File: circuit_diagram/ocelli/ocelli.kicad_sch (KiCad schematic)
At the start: 114 parts, among them J1 Conn_01x06, J2 Conn_01x06, J3 Conn_01x06, J4 Conn_01x06, J5 Conn_01x08, J6 Conn_01x02, J7 Conn_01x02, Q1 BSS138, Q10 BSS138, Q2 ST-1KL3A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

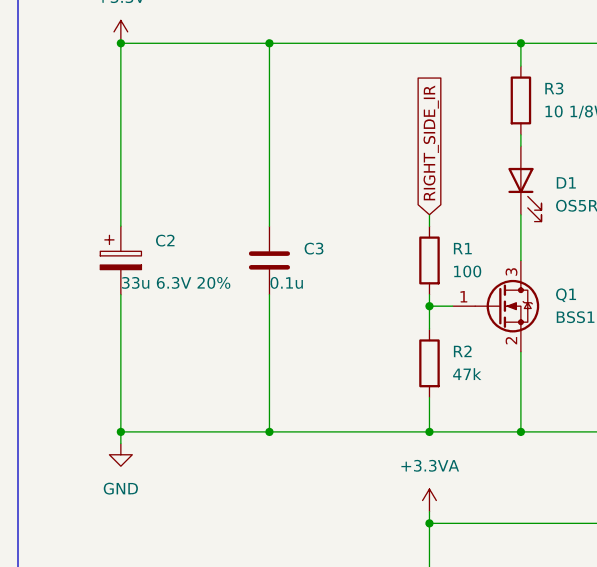
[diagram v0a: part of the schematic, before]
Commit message: 使用するコンデンサを変更
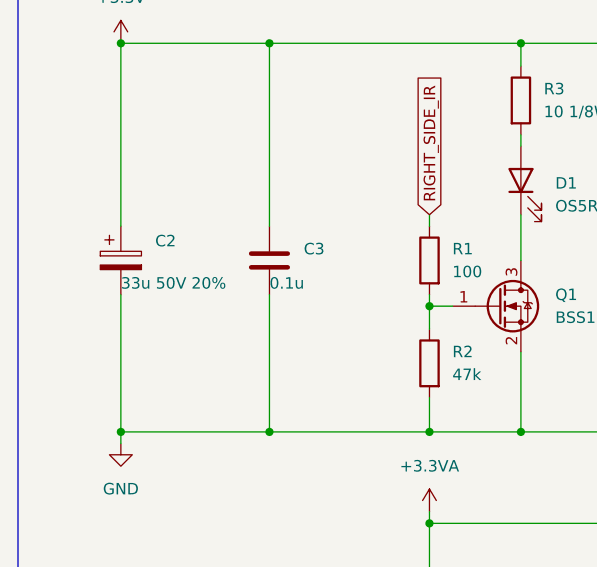
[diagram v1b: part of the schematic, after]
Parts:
- C2: value 33u 6.3V 20% -> 33u 50V 20%; url https://www.digikey.jp/ja/products/detail/murata-electronic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 -> https://akizukidenshi.com/catalog/g/gP-16749/
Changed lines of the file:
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@@
       (effects (font (size 1.27 1.27)) (justify left))
     )
-    (property "Value" "33u 6.3V 20%" (id 1) (at 24.13 96.52 0)
+    (property "Value" "33u 50V 20%" (id 1) (at 24.13 96.52 0)
       (effects (font (size 1.27 1.27)) (justify left))
     )
@@
       (effects (font (size 1.27 1.27)) hide)
     )
-    (property "url" "https://www.digikey.jp/ja/products/detail/murata-electronics/GRT32DR60J336ME01K/13904806" (id 4) (at 24.13 93.98 0)
+    (property "url" "https://akizukidenshi.com/catalog/g/gP-16749/" (id 4) (at 24.13 93.98 0)
       (effects (font (size 1.27 1.27)) hide)
     )
@@
     )
     (path "/6ec1fbce-5ed9-49a9-b67b-d64bef25ff62"
-      (reference "C2") (unit 1) (value "33u 6.3V 20%") (footprint "")
+      (reference "C2") (unit 1) (value "33u 50V 20%") (footprint "")
     )
     (path "/230be6a4-af26-49e4-a244-e2dbf0a97ea4"

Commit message: フットプリント割当完了
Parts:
- BT1: footprint (none) -> ocelli_lib:pad_01x02
- C2: footprint (none) -> Capacitor_SMD:CP_Elec_6.3x7.7
- D1, D2, D3, D5: footprint (none) -> LED_THT:LED_D5.0mm_Horizontal_O1.27mm_Z3.0mm; url (none) -> https://akizukidenshi.com/catalog/g/gI-04768/
- D4, D6, D7: value LED -> OSBL1608C1A; url (none) -> https://akizukidenshi.com/catalog/g/gI-03982/
- D8, D9: value LED -> OSYL1608C1A; url (none) -> https://akizukidenshi.com/catalog/g/gI-03984/
- FB1: footprint (none) -> Inductor_SMD:L_0603_1608Metric_Pad1.05x0.95mm_HandSolder; url (none) -> https://www.digikey.jp/ja/products/detail/bourns-inc/MZ1608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
- J1, J2, J3, J4: footprint (none) -> ocelli_lib:encoder_board_pad; url (none) -> none
- J5: footprint (none) -> Connector_PinSocket_1.27mm:PinSocket_1x08_P1.27mm_Vertical
- J6, J7: footprint (none) -> ocelli_lib:pad_01x02; url (none) -> none
- LS1: footprint (none) -> Buzzer_Beeper:Buzzer_Murata_PKMCS0909E; url (none) -> https://akizukidenshi.com/catalog/g/gP-14238/
- Q1, Q10, Q5, Q7, Q9: footprint (none) -> Package_TO_SOT_SMD:SOT-23; url (none) -> https://akizukidenshi.com/catalog/g/gI-04232/
- Q2, Q4, Q6, Q8: footprint (none) -> LED_THT:LED_D5.0mm_Horizontal_O3.81mm_Z9.0mm; url (none) -> https://www.rt-shop.jp/index.php?main_page=product_info&pro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
- Q3: footprint (none) -> Package_TO_SOT_SMD:TO-252-2; url (none) -> https://akizukidenshi.com/catalog/g/gI-13964/
- RV1: footprint (none) -> ocelli_lib:ST4ETB103
- SW1: footprint (none) -> ocelli_lib:SSSS213202; url (none) -> https://akizukidenshi.com/catalog/g/gP-05043/
- SW2, SW3, SW4: value TS-06104 -> TVAF06-A020B-R; footprint (none) -> ocelli_lib:TVAF06-A020B-R; symbol Switch:SW_MEC_5E -> Switch:SW_MEC_5G; url (none) -> https://akizukidenshi.com/catalog/g/gP-14888/
- SW5, SW6: value SW_Push -> TVAF06-A020B-R; footprint (none) -> ocelli_lib:TVAF06-A020B-R; url (none) -> https://akizukidenshi.com/catalog/g/gP-14888/
- U1: footprint (none) -> Package_TO_SOT_SMD:TO-252-2; url (none) -> https://akizukidenshi.com/catalog/g/gI-11299/
- U2, U3: url (none) -> https://www.mouser.jp/ProductDetail/ams/AS5055A-BQFT?qs=Ifo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
- U4: footprint (none) -> Package_DFN_QFN:HVQFN-24-1EP_4x4mm_P0.5mm_EP2.1x2.1mm; url (none) -> https://www.mouser.jp/ProductDetail/TDK-InvenSense/ICM-2064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
- U5: url (none) -> https://akizukidenshi.com/catalog/g/gI-13219/
- U6: footprint (none) -> ocelli_lib:DRV8835; url (none) -> https://akizukidenshi.com/catalog/g/gK-09848/
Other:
- moved on the sheet: C18, J5, R24, R31, R32, R33, SW5, SW6

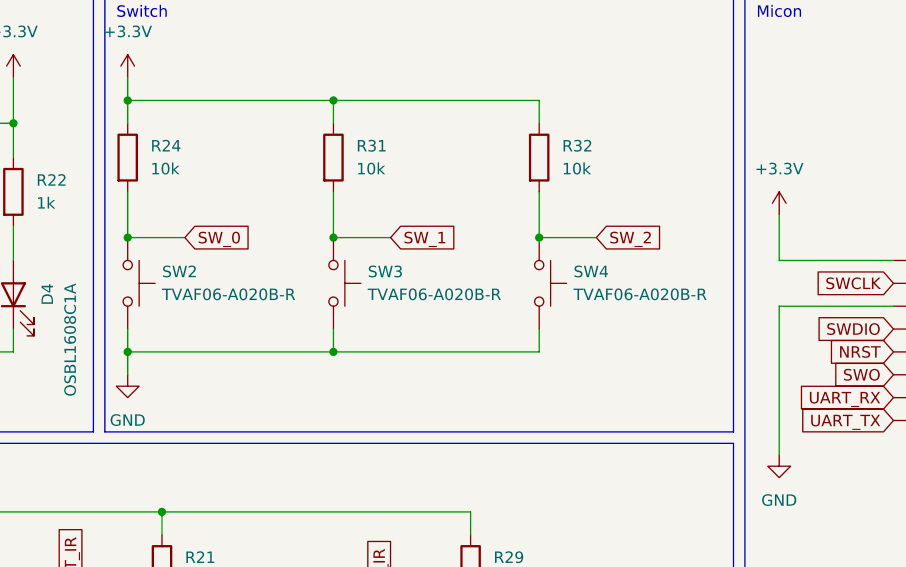
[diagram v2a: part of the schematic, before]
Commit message: モータマウント等のスケッチ追加
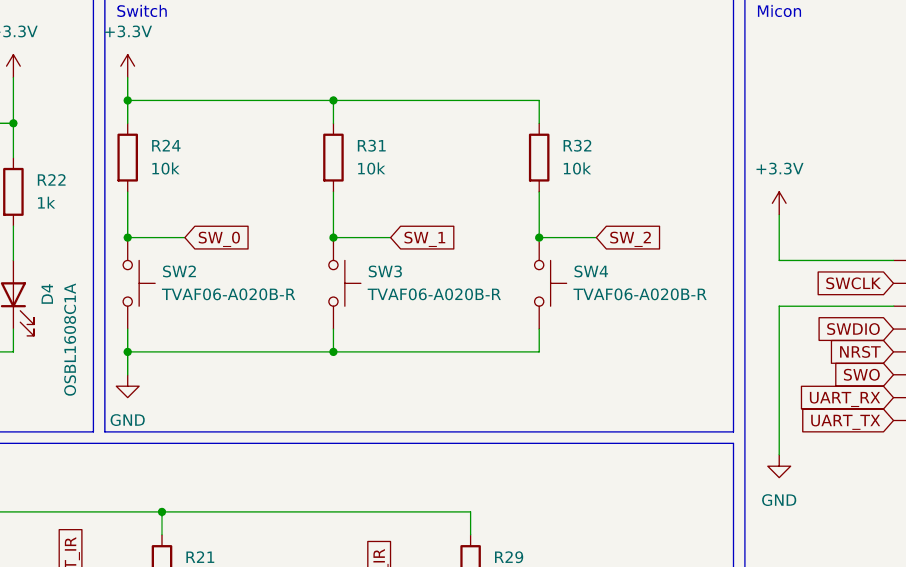
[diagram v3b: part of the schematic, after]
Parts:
- removed SW2, SW3, SW4: TVAF06-A020B-R, ocelli_lib:TVAF06-A020B-R, symbol Switch:SW_MEC_5G
- added SW2, SW3, SW4: TVAF06-A020B-R, ocelli_lib:TVAF06-A020B-R, symbol Switch:SW_Push
- Q2, Q4, Q6, Q8: footprint LED_THT:LED_D5.0mm_Horizontal_O3.81mm_Z9.0mm -> ocelli_lib:ST-1KL3A
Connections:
- net GND: now also SW2.2, SW3.2, SW4.2
- net SW_0: now also SW2.1
- net SW_1: now also SW3.1
- net SW_2: now also SW4.1
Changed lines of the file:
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@@
   (junction (at 106.68 161.29) (diameter 0) (color 0 0 0 0)
   )
-  (junction (at 133.35 39.37) (diameter 0) (color 0 0 0 0)
-  )
   (junction (at 256.54 127) (diameter 0) (color 0 0 0 0)
   )
@@
   (junction (at 140.97 161.29) (diameter 0) (color 0 0 0 0)
   )
+  (junction (at 133.35 39.37) (diameter 0) (color 0 0 0 0)
+  )
   (junction (at 85.09 26.67) (diameter 0) (color 0 0 0 0)
   )
@@
   (junction (at 367.03 132.08) (diameter 0) (color 0 0 0 0)
   )
-  (junction (at 156.21 39.37) (diameter 0) (color 0 0 0 0)
-  )
   (junction (at 241.3 88.9) (diameter 0) (color 0 0 0 0)
   )
@@
   (junction (at 364.49 165.1) (diameter 0) (color 0 0 0 0)
   )
+  (junction (at 156.21 39.37) (diameter 0) (color 0 0 0 0)
+  )
   (junction (at 345.44 171.45) (diameter 0) (color 0 0 0 0)
   )
@@
     (pin "1")
   )
+  (symbol (lib_id "Switch:SW_Push") (at 156.21 44.45 270) (unit 1)
+    (in_bom yes) (on_board yes) (fields_autoplaced)
+    (property "Reference" "SW3" (id 0) (at 160.02 43.1799 90)
+      (effects (font (size 1.27 1.27)) (justify left))
+    )
+    (property "Value" "TVAF06-A020B-R" (id 1) (at 160.02 45.7199 90)
+      (effects (font (size 1.27 1.27)) (justify left))
+    )
+    (property "Footprint" "ocelli_lib:TVAF06-A020B-R" (id 2) (at 161.29 44.45 0)
+      (effects (font (size 1.27 1.27)) hide)
+    )
+    (property "Datasheet" "~" (id 3) (at 161.29 44.45 0)
+      (effects (font (size 1.27 1.27)) hide)
+    )
+    (property "url" "https://akizukidenshi.com/catalog/g/gP-14888/" (id 4) (at 156.21 44.45 0)
+      (effects (font (size 1.27 1.27)) hide)
+    )
+    (pin "1")
+    (pin "2")
+  )
   (symbol (lib_id "Device:C") (at 107.95 39.37 0) (unit 1)
     (in_bom yes) (on_board yes)
@@
       (effects (font (size 1.27 1.27)) (justify left))
     )
-    (property "Footprint" "LED_THT:LED_D5.0mm_Horizontal_O3.81mm_Z9.0mm" (id 2) (at 163.83 134.62 0)
+    (property "Footprint" "ocelli_lib:ST-1KL3A" (id 2) (at 163.83 134.62 0)
       (effects (font (size 1.27 1.27)) hide)
     )
@@
     (pin "2")
   )
-  (symbol (lib_id "Switch:SW_MEC_5G") (at 179.07 44.45 270) (unit 1)
-    (in_bom yes) (on_board yes)
-    (property "Reference" "SW4" (id 0) (at 182.88 43.18 90)
-      (effects (font (size 1.27 1.27)) (justify left))
-    )
-    (property "Value" "TVAF06-A020B-R" (id 1) (at 182.88 45.72 90)
-      (effects (font (size 1.27 1.27)) (justify left))
-    )
-    (property "Footprint" "ocelli_lib:TVAF06-A020B-R" (id 2) (at 184.15 44.45 0)
-      (effects (font (size 1.27 1.27)) hide)
-    )
-    (property "Datasheet" "http://www.apem.com/int/index.php?controller=attachment&id_attachment=488" (id 3) (at 184.15 44.45 0)
-      (effects (font (size 1.27 1.27)) hide)
-    )
-    (property "url" "https://akizukidenshi.com/catalog/g/gP-14888/" (id 4) (at 179.07 44.45 0)
-      (effects (font (size 1.27 1.27)) hide)
-    )
-    (pin "1")
-    (pin "3")
-    (pin "2")
-    (pin "4")
-  )
   (symbol (lib_id "Device:R") (at 68.58 76.2 0) (unit 1)
     (in_bom yes) (on_board yes) (fields_autoplaced)
@@
     (pin "3")
   )
-  (symbol (lib_id "Switch:SW_MEC_5G") (at 133.35 44.45 270) (unit 1)
-    (in_bom yes) (on_board yes)
-    (property "Reference" "SW2" (id 0) (at 137.16 43.18 90)
-      (effects (font (size 1.27 1.27)) (justify left))
-    )
-    (property "Value" "TVAF06-A020B-R" (id 1) (at 137.16 45.72 90)
-      (effects (font (size 1.27 1.27)) (justify left))
-    )
-    (property "Footprint" "ocelli_lib:TVAF06-A020B-R" (id 2) (at 138.43 44.45 0)
-      (effects (font (size 1.27 1.27)) hide)
-    )
-    (property "Datasheet" "http://www.apem.com/int/index.php?controller=attachment&id_attachment=488" (id 3) (at 138.43 44.45 0)
-      (effects (font (size 1.27 1.27)) hide)
-    )
-    (property "url" "https://akizukidenshi.com/catalog/g/gP-14888/" (id 4) (at 133.35 44.45 0)
-      (effects (font (size 1.27 1.27)) hide)
-    )
-    (pin "1")
-    (pin "3")
-    (pin "2")
-    (pin "4")
-  )
   (symbol (lib_id "power:GND") (at 180.34 248.92 0) (unit 1)
     (in_bom yes) (on_board yes) (fields_autoplaced)
@@
     (pin "2")
   )
+  (symbol (lib_id "Switch:SW_Push") (at 179.07 44.45 270) (unit 1)
+    (in_bom yes) (on_board yes) (fields_autoplaced)
+    (property "Reference" "SW4" (id 0) (at 182.88 43.1799 90)
+      (effects (font (size 1.27 1.27)) (justify left))
+    )
+    (property "Value" "TVAF06-A020B-R" (id 1) (at 182.88 45.7199 90)
+      (effects (font (size 1.27 1.27)) (justify left))
+    )
+    (property "Footprint" "ocelli_lib:TVAF06-A020B-R" (id 2) (at 184.15 44.45 0)
+      (effects (font (size 1.27 1.27)) hide)
+    )
+    (property "Datasheet" "~" (id 3) (at 184.15 44.45 0)
+      (effects (font (size 1.27 1.27)) hide)
+    )
+    (property "url" "https://akizukidenshi.com/catalog/g/gP-14888/" (id 4) (at 179.07 44.45 0)
+      (effects (font (size 1.27 1.27)) hide)
+    )
+    (pin "1")
+    (pin "2")
+  )
   (symbol (lib_id "Device:Q_Photo_NPN") (at 55.88 137.16 0) (unit 1)
     (in_bom yes) (on_board yes) (fields_autoplaced)
@@
       (effects (font (size 1.27 1.27)) (justify left))
     )
-    (property "Footprint" "LED_THT:LED_D5.0mm_Horizontal_O3.81mm_Z9.0mm" (id 2) (at 60.96 134.62 0)
+    (property "Footprint" "ocelli_lib:ST-1KL3A" (id 2) (at 60.96 134.62 0)
       (effects (font (size 1.27 1.27)) hide)
     )
@@
     (pin "6")
   )
+  (symbol (lib_id "Switch:SW_Push") (at 133.35 44.45 270) (unit 1)
+    (in_bom yes) (on_board yes) (fields_autoplaced)
+    (property "Reference" "SW2" (id 0) (at 137.16 43.1799 90)
+      (effects (font (size 1.27 1.27)) (justify left))
+    )
+    (property "Value" "TVAF06-A020B-R" (id 1) (at 137.16 45.7199 90)
+      (effects (font (size 1.27 1.27)) (justify left))
+    )
+    (property "Footprint" "ocelli_lib:TVAF06-A020B-R" (id 2) (at 138.43 44.45 0)
+      (effects (font (size 1.27 1.27)) hide)
+    )
+    (property "Datasheet" "~" (id 3) (at 138.43 44.45 0)
+      (effects (font (size 1.27 1.27)) hide)
+    )
+    (property "url" "https://akizukidenshi.com/catalog/g/gP-14888/" (id 4) (at 133.35 44.45 0)
+      (effects (font (size 1.27 1.27)) hide)
+    )
+    (pin "1")
+    (pin "2")
+  )
   (symbol (lib_id "Device:C") (at 226.06 105.41 0) (unit 1)
     (in_bom yes) (on_board yes)
@@
       (effects (font (size 1.27 1.27)) (justify left))
     )
-    (property "Footprint" "LED_THT:LED_D5.0mm_Horizontal_O3.81mm_Z9.0mm" (id 2) (at 95.25 134.62 0)
+    (property "Footprint" "ocelli_lib:ST-1KL3A" (id 2) (at 95.25 134.62 0)
       (effects (font (size 1.27 1.27)) hide)
     )
@@
       (effects (font (size 1.27 1.27)) (justify left))
     )
-    (property "Footprint" "LED_THT:LED_D5.0mm_Horizontal_O3.81mm_Z9.0mm" (id 2) (at 129.54 134.62 0)
+    (property "Footprint" "ocelli_lib:ST-1KL3A" (id 2) (at 129.54 134.62 0)
       (effects (font (size 1.27 1.27)) hide)
     )
@@
     (pin "1")
   )
-  (symbol (lib_id "Switch:SW_MEC_5G") (at 156.21 44.45 270) (unit 1)
-    (in_bom yes) (on_board yes)
-    (property "Reference" "SW3" (id 0) (at 160.02 43.18 90)
-      (effects (font (size 1.27 1.27)) (justify left))
-    )
-    (property "Value" "TVAF06-A020B-R" (id 1) (at 160.02 45.72 90)
-      (effects (font (size 1.27 1.27)) (justify left))
-    )
-    (property "Footprint" "ocelli_lib:TVAF06-A020B-R" (id 2) (at 161.29 44.45 0)
-      (effects (font (size 1.27 1.27)) hide)
-    )
-    (property "Datasheet" "http://www.apem.com/int/index.php?controller=attachment&id_attachment=488" (id 3) (at 161.29 44.45 0)
-      (effects (font (size 1.27 1.27)) hide)
-    )
-    (property "url" "https://akizukidenshi.com/catalog/g/gP-14888/" (id 4) (at 156.21 44.45 0)
-      (effects (font (size 1.27 1.27)) hide)
-    )
-    (pin "1")
-    (pin "3")
-    (pin "2")
-    (pin "4")
-  )
   (symbol (lib_id "power:GND") (at 251.46 67.31 0) (unit 1)
     (in_bom yes) (on_board yes) (fields_autoplaced)
@@
     )
     (path "/4c45e7b5-910f-4a6e-9672-ff25f0fd35cc"
-      (reference "Q2") (unit 1) (value "ST-1KL3A") (footprint "LED_THT:LED_D5.0mm_Horizontal_O3.81mm_Z9.0mm")
+      (reference "Q2") (unit 1) (value "ST-1KL3A") (footprint "ocelli_lib:ST-1KL3A")
     )
     (path "/435dadaa-c7e3-4c4f-bc2c-12a7e04a6abf"
@@
     )
     (path "/78380d7a-7050-4fa4-83b0-a213bce03f9b"
-      (reference "Q4") (unit 1) (value "ST-1KL3A") (footprint "LED_THT:LED_D5.0mm_Horizontal_O3.81mm_Z9.0mm")
+      (reference "Q4") (unit 1) (value "ST-1KL3A") (footprint "ocelli_lib:ST-1KL3A")
     )
     (path "/94ce2d53-3690-4996-b763-8e3b6108af0e"
@@
     )
     (path "/9f5b177c-9103-4a89-b330-896e69e5904b"
-      (reference "Q6") (unit 1) (value "ST-1KL3A") (footprint "LED_THT:LED_D5.0mm_Horizontal_O3.81mm_Z9.0mm")
+      (reference "Q6") (unit 1) (value "ST-1KL3A") (footprint "ocelli_lib:ST-1KL3A")
     )
     (path "/75084031-bbcc-406c-9e18-9391703c81e5"
@@
     )
     (path "/32aec8ec-50f2-4728-8cae-a80e6b28ac7b"
-      (reference "Q8") (unit 1) (value "ST-1KL3A") (footprint "LED_THT:LED_D5.0mm_Horizontal_O3.81mm_Z9.0mm")
+      (reference "Q8") (unit 1) (value "ST-1KL3A") (footprint "ocelli_lib:ST-1KL3A")
     )
     (path "/1e2c13ea-b331-4134-badd-72868480756e"
@@
       (reference "SW1") (unit 1) (value "SW_SPDT") (footprint "ocelli_lib:SSSS213202")
     )
-    (path "/43862056-8f38-4e81-aa22-d1ec7c5a2da3"
+    (path "/58cb58b3-37ed-4568-8a79-346a92967709"
       (reference "SW2") (unit 1) (value "TVAF06-A020B-R") (footprint "ocelli_lib:TVAF06-A020B-R")
     )
-    (path "/f6fb72fb-63c0-4b68-b993-96a8461decb2"
+    (path "/0a2cfeda-4aaf-49a5-8ecc-a99df2e06d58"
       (reference "SW3") (unit 1) (value "TVAF06-A020B-R") (footprint "ocelli_lib:TVAF06-A020B-R")
     )
-    (path "/3efb25df-c3a7-4246-af1c-174de46e1c02"
+    (path "/4b3350b0-8afe-4e06-a639-1386f446f29e"
       (reference "SW4") (unit 1) (value "TVAF06-A020B-R") (footprint "ocelli_lib:TVAF06-A020B-R")
     )

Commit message: 一通りパターンを繋いだ
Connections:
- net DIR_L: now also U5.41 (PA8); no longer U5.43 (PA10)
- net DIR_R: now also U5.43 (PA10); no longer U5.44 (PA11)
- net LEFT_FRONT_AD: now also U5.27 (PB1); no longer U5.26 (PB0)
- net LEFT_SIDE_AD: now also U5.26 (PB0); no longer U5.27 (PB1)
- net PWM_L: now also U5.42 (PA9); no longer U5.41 (PA8)
- net PWM_R: now also U5.44 (PA11); no longer U5.42 (PA9)
- net RIGHT_FRONT_AD: now also U5.24 (PC4); no longer U5.25 (PC5)
- net RIGHT_SIDE_AD: now also U5.25 (PC5); no longer U5.24 (PC4)
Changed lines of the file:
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@@
     )
   )
-  (global_label "RIGHT_SIDE_AD" (shape input) (at 233.68 185.42 180) (fields_autoplaced)
-    (effects (font (size 1.27 1.27)) (justify right))
-    (property "Intersheet References" "${INTERSHEET_REFS}" (id 0) (at 217.2969 185.4994 0)
+  (global_label "RIGHT_SIDE_AD" (shape input) (at 233.68 187.96 180) (fields_autoplaced)
+    (effects (font (size 1.27 1.27)) (justify right))
+    (property "Intersheet References" "${INTERSHEET_REFS}" (id 0) (at 217.2969 188.0394 0)
       (effects (font (size 1.27 1.27)) (justify right) hide)
     )
@@
     )
   )
-  (global_label "LEFT_FRONT_AD" (shape input) (at 269.24 175.26 0) (fields_autoplaced)
-    (effects (font (size 1.27 1.27)) (justify left))
-    (property "Intersheet References" "${INTERSHEET_REFS}" (id 0) (at 286.1674 175.1806 0)
-      (effects (font (size 1.27 1.27)) (justify left) hide)
-    )
-  )
-  (global_label "RIGHT_FRONT_AD" (shape input) (at 233.68 187.96 180) (fields_autoplaced)
-    (effects (font (size 1.27 1.27)) (justify right))
-    (property "Intersheet References" "${INTERSHEET_REFS}" (id 0) (at 215.5431 188.0394 0)
+  (global_label "LEFT_FRONT_AD" (shape input) (at 269.24 177.8 0) (fields_autoplaced)
+    (effects (font (size 1.27 1.27)) (justify left))
+    (property "Intersheet References" "${INTERSHEET_REFS}" (id 0) (at 286.1674 177.7206 0)
+      (effects (font (size 1.27 1.27)) (justify left) hide)
+    )
+  )
+  (global_label "RIGHT_FRONT_AD" (shape input) (at 233.68 185.42 180) (fields_autoplaced)
+    (effects (font (size 1.27 1.27)) (justify right))
+    (property "Intersheet References" "${INTERSHEET_REFS}" (id 0) (at 215.5431 185.4994 0)
       (effects (font (size 1.27 1.27)) (justify right) hide)
     )
@@
     )
   )
-  (global_label "DIR_L" (shape input) (at 269.24 157.48 0) (fields_autoplaced)
-    (effects (font (size 1.27 1.27)) (justify left))
-    (property "Intersheet References" "${INTERSHEET_REFS}" (id 0) (at 276.7936 157.4006 0)
+  (global_label "DIR_L" (shape input) (at 269.24 152.4 0) (fields_autoplaced)
+    (effects (font (size 1.27 1.27)) (justify left))
+    (property "Intersheet References" "${INTERSHEET_REFS}" (id 0) (at 276.7936 152.3206 0)
       (effects (font (size 1.27 1.27)) (justify left) hide)
     )
@@
     )
   )
-  (global_label "LEFT_SIDE_AD" (shape input) (at 269.24 177.8 0) (fields_autoplaced)
-    (effects (font (size 1.27 1.27)) (justify left))
-    (property "Intersheet References" "${INTERSHEET_REFS}" (id 0) (at 284.4136 177.7206 0)
+  (global_label "LEFT_SIDE_AD" (shape input) (at 269.24 175.26 0) (fields_autoplaced)
+    (effects (font (size 1.27 1.27)) (justify left))
+    (property "Intersheet References" "${INTERSHEET_REFS}" (id 0) (at 284.4136 175.1806 0)
       (effects (font (size 1.27 1.27)) (justify left) hide)
     )
@@
     )
   )
-  (global_label "PWM_R" (shape input) (at 269.24 154.94 0) (fields_autoplaced)
-    (effects (font (size 1.27 1.27)) (justify left))
-    (property "Intersheet References" "${INTERSHEET_REFS}" (id 0) (at 278.0636 154.8606 0)
+  (global_label "PWM_R" (shape input) (at 269.24 160.02 0) (fields_autoplaced)
+    (effects (font (size 1.27 1.27)) (justify left))
+    (property "Intersheet References" "${INTERSHEET_REFS}" (id 0) (at 278.0636 159.9406 0)
       (effects (font (size 1.27 1.27)) (justify left) hide)
     )
@@
     )
   )
-  (global_label "PWM_L" (shape input) (at 269.24 152.4 0) (fields_autoplaced)
-    (effects (font (size 1.27 1.27)) (justify left))
-    (property "Intersheet References" "${INTERSHEET_REFS}" (id 0) (at 277.8217 152.3206 0)
+  (global_label "PWM_L" (shape input) (at 269.24 154.94 0) (fields_autoplaced)
+    (effects (font (size 1.27 1.27)) (justify left))
+    (property "Intersheet References" "${INTERSHEET_REFS}" (id 0) (at 277.8217 154.8606 0)
       (effects (font (size 1.27 1.27)) (justify left) hide)
     )
@@
     )
   )
-  (global_label "DIR_R" (shape input) (at 269.24 160.02 0) (fields_autoplaced)
-    (effects (font (size 1.27 1.27)) (justify left))
-    (property "Intersheet References" "${INTERSHEET_REFS}" (id 0) (at 277.0355 159.9406 0)
-      (effects (font (size 1.27 1.27)) (justify left) hide)
-    )
+  (global_label "DIR_R" (shape input) (at 269.24 157.48 0) (fields_autoplaced)
+    (effects (font (size 1.27 1.27)) (justify left))
+    (property "Intersheet References" "${INTERSHEET_REFS}" (id 0) (at 277.0355 157.4006 0)
+      (effects (font (size 1.27 1.27)) (justify left) hide)
+    )
